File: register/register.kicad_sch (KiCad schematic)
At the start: 13 parts

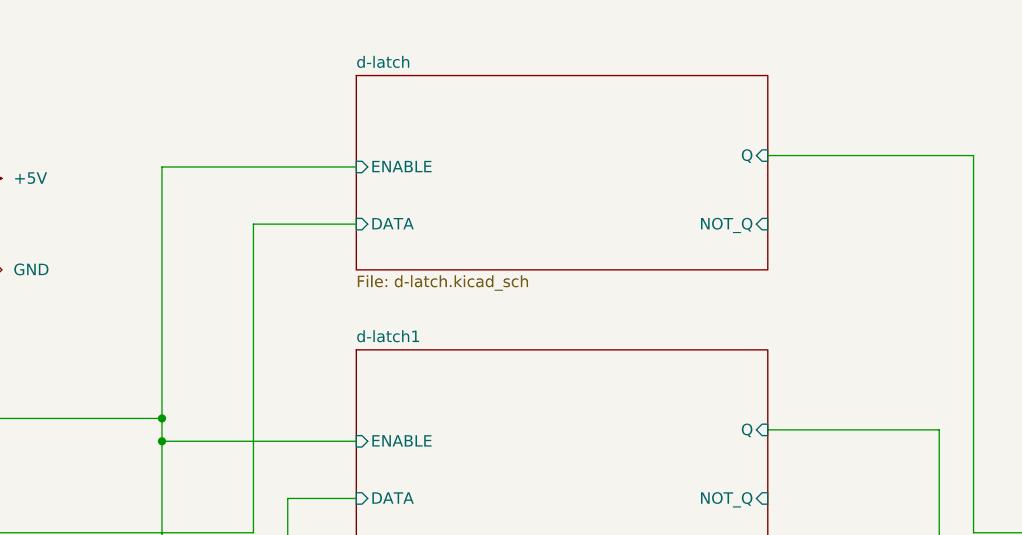
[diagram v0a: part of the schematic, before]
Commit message: Use IC circuits in adder circuit
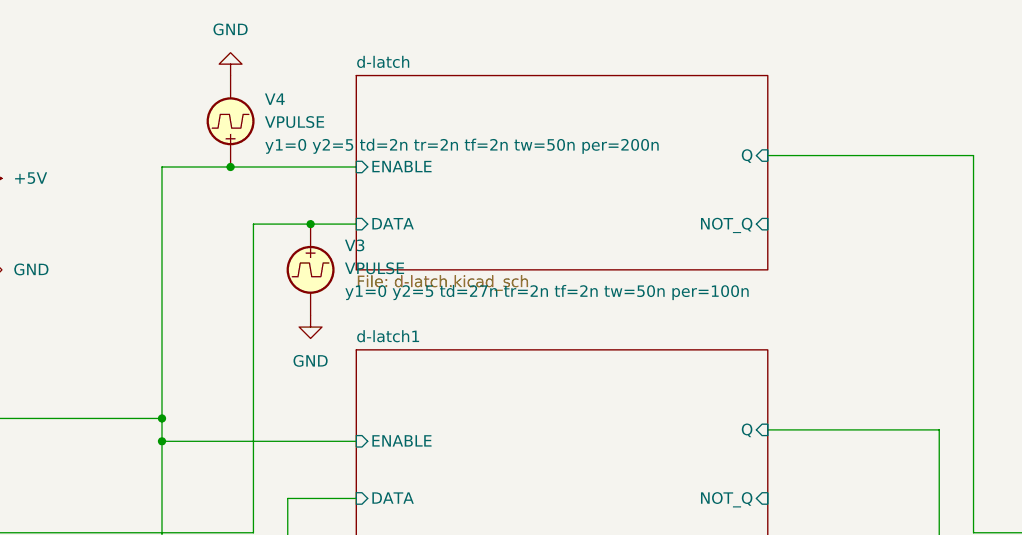
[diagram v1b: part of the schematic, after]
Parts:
- added V3, V4: VPULSE, symbol Simulation_SPICE:VPULSE
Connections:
- net +5V: now also V4.1
- net GND: now also V3.2, V4.2
- net d-latch/DATA: now also V3.1
